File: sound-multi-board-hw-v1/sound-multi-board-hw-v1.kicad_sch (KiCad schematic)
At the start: 39 parts, among them J1 USB_C_Receptacle_USB2.0_16P, J11 SWD, J2 Micro_SD_Card_Det1, SW1 SW_Push, SW2 SW_Push, U1 NAU88C22, U10 STM32F405RGTx, U2 ESP32-WROOM-32, U3 USB3300-EZK, Y1 12MHz 12pF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

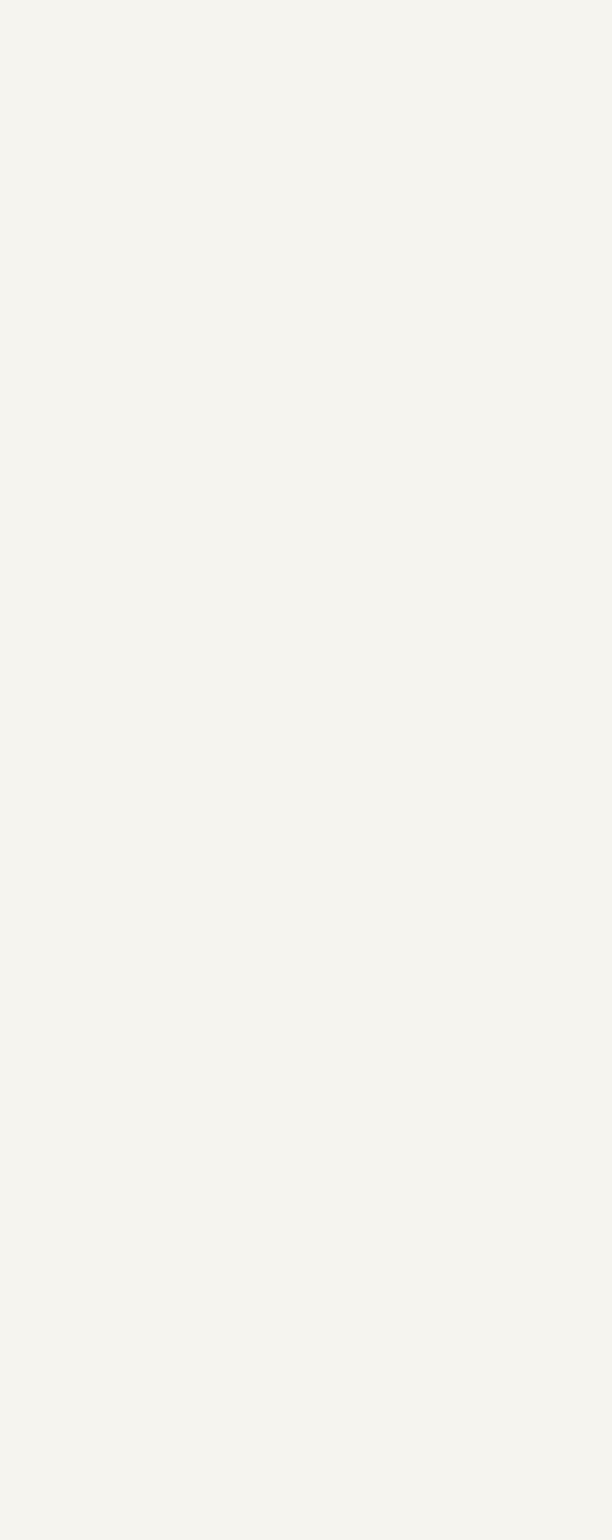
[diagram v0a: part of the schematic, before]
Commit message: added gd32 with external ram
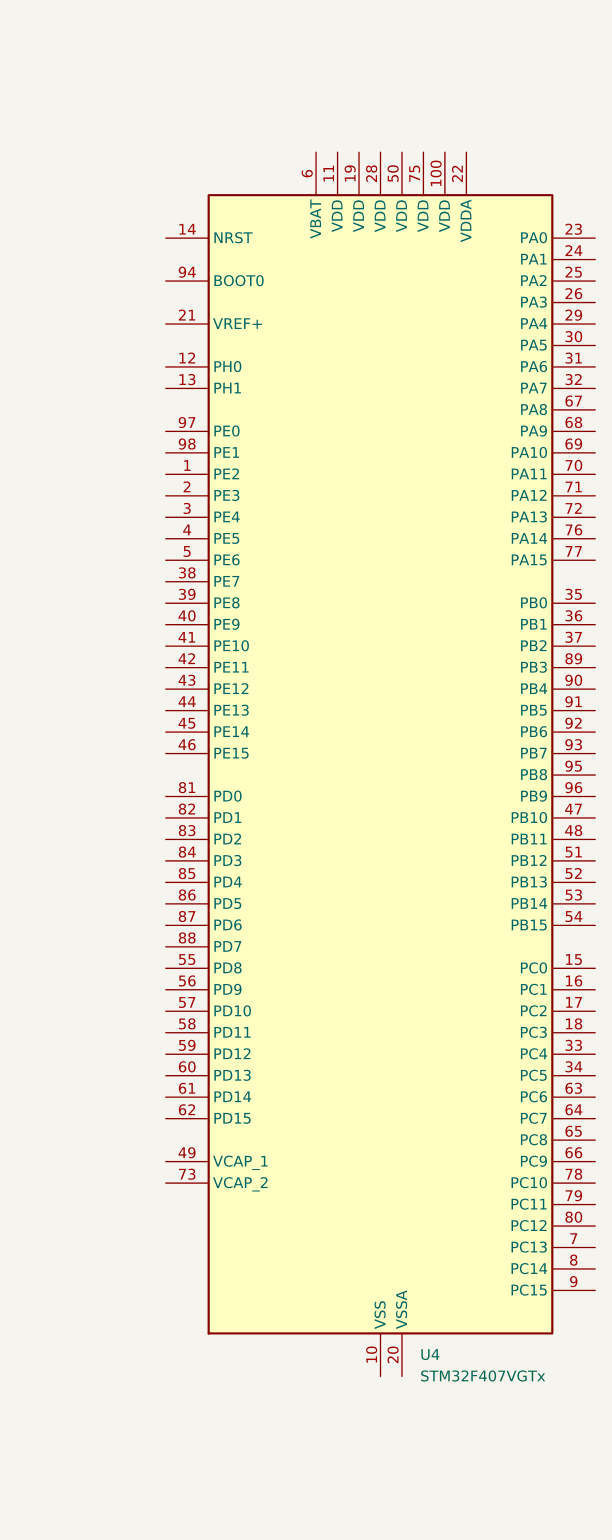
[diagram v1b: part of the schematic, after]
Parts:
- added U4: STM32F407VGTx, Package_QFP:LQFP-100_14x14mm_P0.5mm, symbol MCU_ST_STM32F4:STM32F407VGTx
- J1: footprint (none) -> Connector_USB:USB_C_Receptacle_XKB_U262-16XN-4BVC11
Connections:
- new net: U4.10 (VSS), U4.27 (VSS), U4.74 (VSS), U4.99 (VSS)

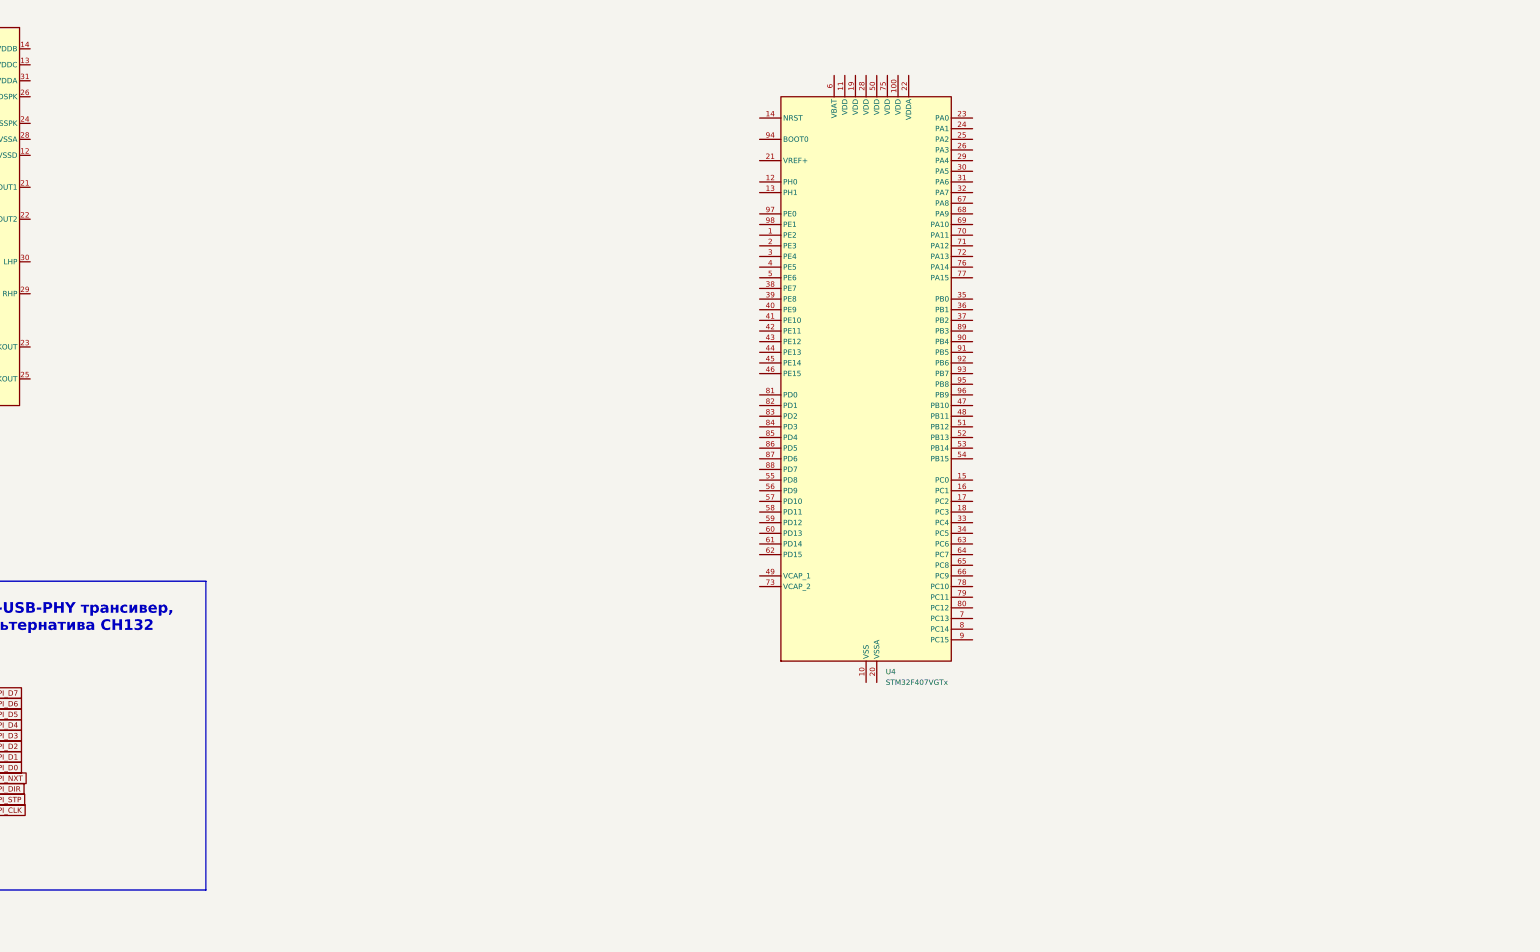
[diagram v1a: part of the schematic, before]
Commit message: choose between lqfp100 and 144
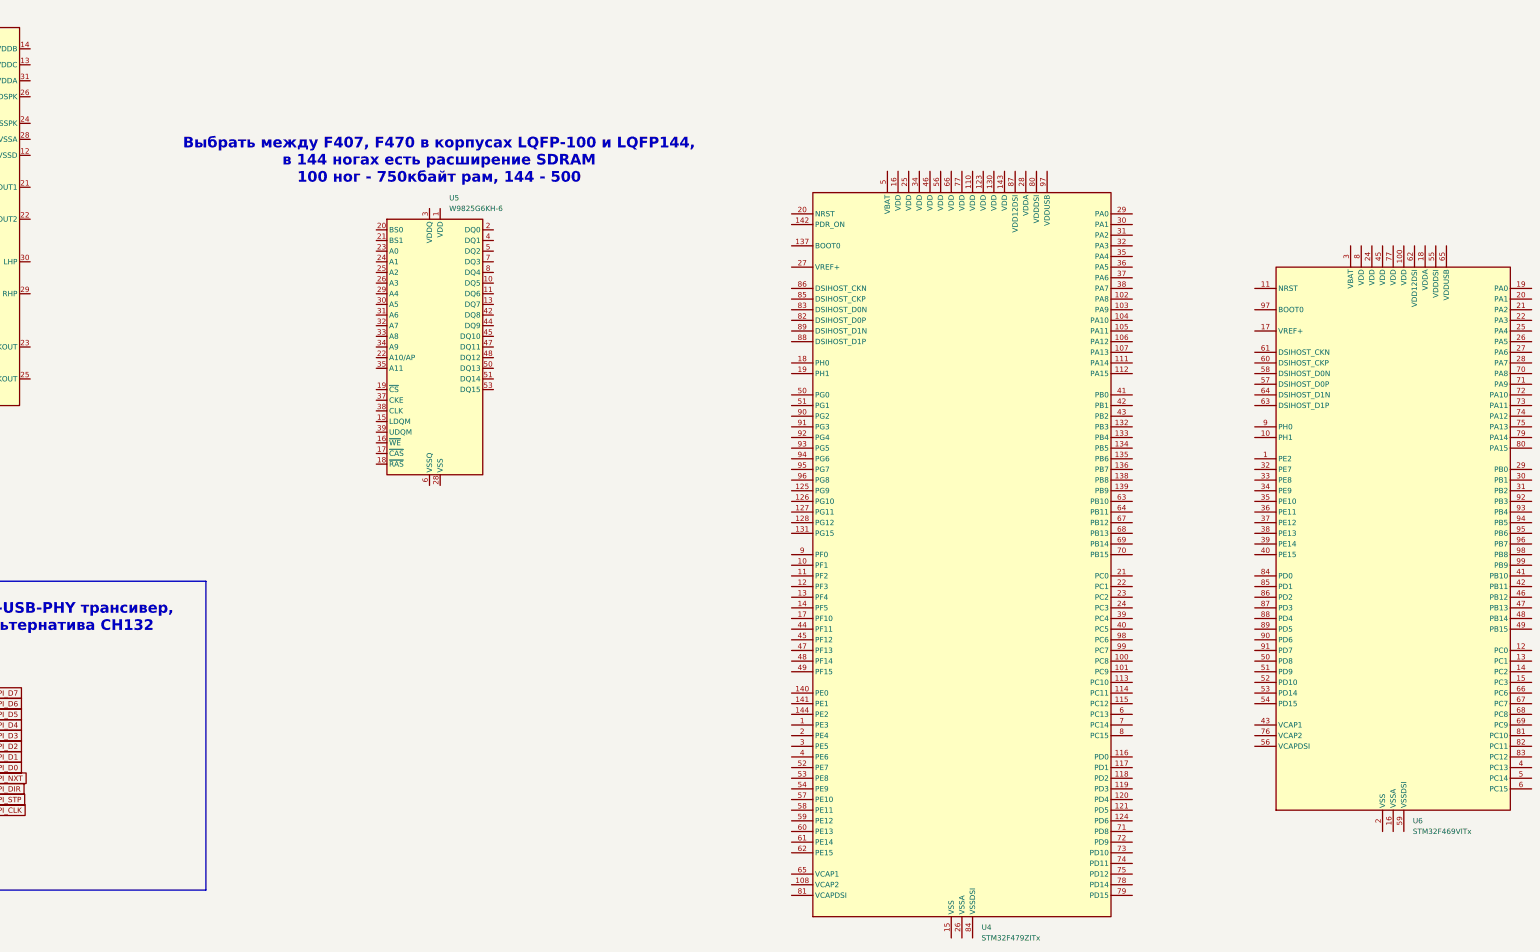
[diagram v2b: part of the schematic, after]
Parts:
- removed U4: STM32F407VGTx, Package_QFP:LQFP-100_14x14mm_P0.5mm, symbol MCU_ST_STM32F4:STM32F407VGTx
- added U4: STM32F479ZITx, Package_QFP:LQFP-144_20x20mm_P0.5mm, symbol MCU_ST_STM32F4:STM32F479ZITx
- added U5: W9825G6KH-6, Package_SO:TSOP-II-54_22.2x10.16mm_P0.8mm, symbol Memory_RAM:W9812G6KH-6
- added U6: STM32F469VITx, Package_QFP:LQFP-100_14x14mm_P0.5mm, symbol MCU_ST_STM32F4:STM32F469VITx
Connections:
- new net: U4.109 (VSS), U4.122 (VSS), U4.129 (VSS), U4.15 (VSS), U4.33 (VSS), U4.55 (VSS), U4.76 (VSS)
- new net: U6.2 (VSS), U6.23 (VSS), U6.44 (VSS), U6.7 (VSS), U6.78 (VSS)
- new net: U5.1 (VDD), U5.14 (VDD), U5.27 (VDD)
- new net: U5.12 (VSSQ), U5.46 (VSSQ), U5.52 (VSSQ), U5.6 (VSSQ)
- new net: U5.28 (VSS), U5.41 (VSS), U5.54 (VSS)
- new net: U5.3 (VDDQ), U5.43 (VDDQ), U5.49 (VDDQ), U5.9 (VDDQ)
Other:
- note added: "Выбрать между F407, F470 в корпусах LQFP-100 и LQFP144, в 144 ногах есть расширение SDRAM 100 ног - 750кбайт рам, 144 - 500"
